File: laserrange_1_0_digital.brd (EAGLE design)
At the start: 29.5 x 54.6 mm, 32 parts, among them U1 STM32F10XRXT6

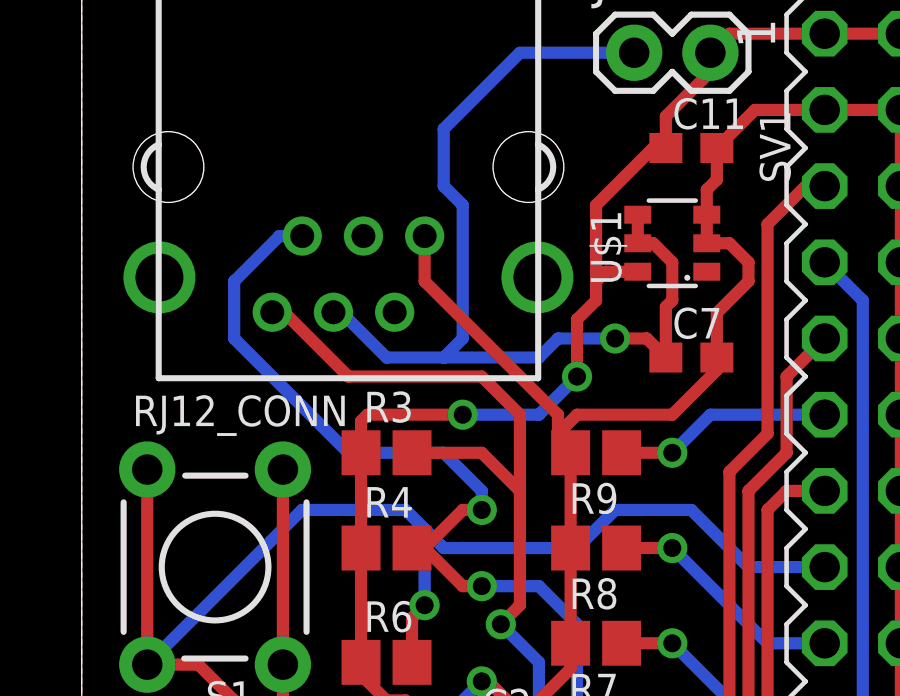
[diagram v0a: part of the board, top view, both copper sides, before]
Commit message: Fixed the RJ12 connector footpad connections
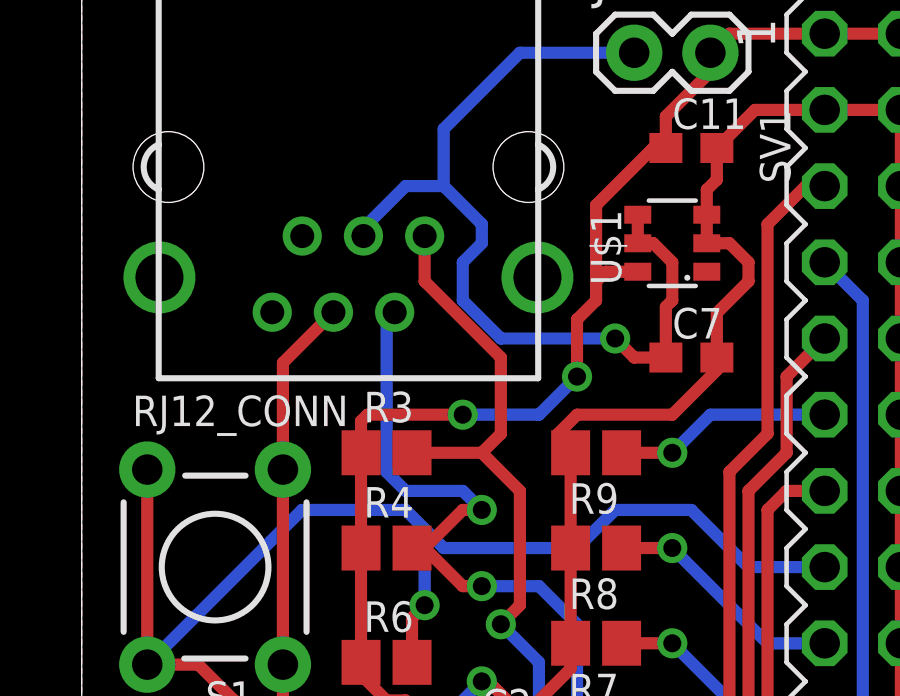
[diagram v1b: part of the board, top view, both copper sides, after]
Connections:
- net 4.3V: now also RJ12_CONN.3; no longer RJ12_CONN.4
- net GND: now also RJ12_CONN.4; no longer RJ12_CONN.1
- net I2C_CLOCK: now also RJ12_CONN.2; no longer RJ12_CONN.5
- net I2C_DATA: now also RJ12_CONN.1; no longer RJ12_CONN.6
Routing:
- net I2C_CLOCK: track 31.5 -> 24.8 mm
- net I2C_DATA: track 32.2 -> 28.6 mm
- net 4.3V: track 33.4 -> 30.6 mm
- net GND: track 173.0 -> 170.5 mm
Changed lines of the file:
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@@
 <signals>
 <signal name="4.3V">
-<contactref element="RJ12_CONN" pad="4"/>
 <contactref element="U$1" pad="5"/>
 <contactref element="C7" pad="1"/>
@@
 <wire x1="19.685" y1="43.815" x2="19.47" y2="43.6" width="0.4064" layer="1"/>
 <wire x1="19.47" y1="41.91" x2="19.47" y2="43.6" width="0.4064" layer="1"/>
-<wire x1="8.39" y1="43.42" x2="8.65" y2="43.42" width="0.4064" layer="16"/>
-<wire x1="8.65" y1="43.42" x2="10.16" y2="41.91" width="0.4064" layer="16"/>
-<wire x1="10.16" y1="41.91" x2="12.065" y2="41.91" width="0" layer="19" extent="1-16"/>
-<wire x1="10.16" y1="41.91" x2="12.065" y2="41.91" width="0.4064" layer="16"/>
-<wire x1="12.065" y1="41.91" x2="15.24" y2="41.91" width="0.4064" layer="16"/>
-<wire x1="15.24" y1="41.91" x2="15.875" y2="42.545" width="0.4064" layer="16"/>
-<wire x1="15.875" y1="42.545" x2="17.78" y2="42.545" width="0.4064" layer="16"/>
-<via x="17.78" y="42.545" extent="1-16" drill="0.6"/>
-<wire x1="17.78" y1="42.545" x2="18.835" y2="42.545" width="0.4064" layer="1"/>
-<wire x1="18.835" y1="42.545" x2="19.47" y2="41.91" width="0.4064" layer="1"/>
 <contactref element="U$1" pad="4"/>
 <wire x1="18.535" y1="45.72" x2="18.535" y2="46.67" width="0.4064" layer="1"/>
 <contactref element="JP2" pad="1"/>
+<contactref element="RJ12_CONN" pad="3"/>
+<wire x1="9.39" y1="45.96" x2="9.39" y2="46.22" width="0.4064" layer="16"/>
+<wire x1="9.39" y1="46.22" x2="10.795" y2="47.625" width="0.4064" layer="16"/>
+<wire x1="10.795" y1="47.625" x2="12.065" y2="47.625" width="0.4064" layer="16"/>
+<wire x1="12.065" y1="47.625" x2="13.335" y2="46.355" width="0.4064" layer="16"/>
+<wire x1="13.335" y1="46.355" x2="13.335" y2="45.72" width="0.4064" layer="16"/>
+<wire x1="13.335" y1="45.72" x2="12.7" y2="45.085" width="0.4064" layer="16"/>
+<wire x1="12.7" y1="45.085" x2="12.7" y2="43.815" width="0.4064" layer="16"/>
+<wire x1="12.7" y1="43.815" x2="13.97" y2="42.545" width="0.4064" layer="16"/>
+<wire x1="13.97" y1="42.545" x2="17.78" y2="42.545" width="0.4064" layer="16"/>
 <wire x1="18.415" y1="52.07" x2="14.605" y2="52.07" width="0.4064" layer="16"/>
 <wire x1="14.605" y1="52.07" x2="12.065" y2="49.53" width="0.4064" layer="16"/>
-<wire x1="12.7" y1="42.545" x2="12.065" y2="41.91" width="0" layer="19" extent="1-16"/>
 <wire x1="12.065" y1="49.53" x2="12.065" y2="47.625" width="0.4064" layer="16"/>
-<wire x1="12.065" y1="47.625" x2="12.7" y2="46.99" width="0.4064" layer="16"/>
-<wire x1="12.7" y1="46.99" x2="12.7" y2="42.545" width="0.4064" layer="16"/>
-<wire x1="12.7" y1="42.545" x2="12.065" y2="41.91" width="0.4064" layer="16"/>
-<wire x1="12.065" y1="41.91" x2="12.7" y2="42.545" width="0" layer="19" extent="1-16"/>
+<via x="17.78" y="42.545" extent="1-16" drill="0.6"/>
+<wire x1="19.47" y1="41.91" x2="18.415" y2="41.91" width="0.4064" layer="1"/>
+<wire x1="18.415" y1="41.91" x2="17.78" y2="42.545" width="0.4064" layer="1"/>
 </signal>
 <signal name="I2C_CLOCK">
-<contactref element="RJ12_CONN" pad="5"/>
 <contactref element="U1" pad="58"/>
 <contactref element="R4" pad="2"/>
@@
 <wire x1="16.51" y1="29.21" x2="16.51" y2="33.02" width="0.4064" layer="16"/>
 <via x="13.335" y="34.29" extent="1-16" drill="0.6"/>
-<wire x1="7.35" y1="45.96" x2="6.59" y2="45.96" width="0.4064" layer="16"/>
-<wire x1="6.59" y1="45.96" x2="5.08" y2="44.45" width="0.4064" layer="16"/>
-<wire x1="5.08" y1="44.45" x2="5.08" y2="42.545" width="0.4064" layer="16"/>
-<wire x1="5.08" y1="42.545" x2="8.89" y2="38.735" width="0.4064" layer="16"/>
-<wire x1="8.89" y1="38.735" x2="12.065" y2="38.735" width="0.4064" layer="16"/>
-<wire x1="12.065" y1="38.735" x2="13.335" y2="37.465" width="0.4064" layer="16"/>
 <wire x1="13.335" y1="34.29" x2="15.24" y2="34.29" width="0.4064" layer="16"/>
 <wire x1="15.24" y1="34.29" x2="16.51" y2="33.02" width="0.4064" layer="16"/>
@@
 <wire x1="11.43" y1="35.56" x2="12.7" y2="34.29" width="0.4064" layer="1"/>
 <wire x1="12.7" y1="34.29" x2="13.335" y2="34.29" width="0.4064" layer="1"/>
-<wire x1="13.335" y1="37.465" x2="13.335" y2="36.83" width="0.4064" layer="16"/>
 <via x="13.335" y="36.83" extent="1-16" drill="0.6"/>
 <wire x1="11.43" y1="35.56" x2="12.7" y2="36.83" width="0.4064" layer="1"/>
 <wire x1="12.7" y1="36.83" x2="13.335" y2="36.83" width="0.4064" layer="1"/>
+<contactref element="RJ12_CONN" pad="2"/>
+<wire x1="10.43" y1="43.42" x2="10.16" y2="43.15" width="0.4064" layer="16"/>
+<wire x1="10.16" y1="43.15" x2="10.16" y2="38.1" width="0.4064" layer="16"/>
+<wire x1="10.16" y1="38.1" x2="10.795" y2="37.465" width="0.4064" layer="16"/>
+<wire x1="10.795" y1="37.465" x2="12.7" y2="37.465" width="0.4064" layer="16"/>
+<wire x1="12.7" y1="37.465" x2="13.335" y2="36.83" width="0.4064" layer="16"/>
 </signal>
 <signal name="I2C_DATA">
-<contactref element="RJ12_CONN" pad="6"/>
 <contactref element="U1" pad="59"/>
 <contactref element="R3" pad="2"/>
@@
 <via x="13.97" y="33.02" extent="1-16" drill="0.6"/>
 <wire x1="15.875" y1="27.94" x2="15.875" y2="24.765" width="0.4064" layer="16"/>
-<wire x1="6.35" y1="43.42" x2="6.745" y2="43.42" width="0.4064" layer="1"/>
-<wire x1="14.605" y1="37.465" x2="14.605" y2="40.005" width="0.4064" layer="1"/>
-<wire x1="14.605" y1="40.005" x2="13.335" y2="41.275" width="0.4064" layer="1"/>
-<wire x1="13.335" y1="41.275" x2="8.89" y2="41.275" width="0.4064" layer="1"/>
-<wire x1="8.89" y1="41.275" x2="6.745" y2="43.42" width="0.4064" layer="1"/>
 <wire x1="15.875" y1="27.94" x2="15.24" y2="28.575" width="0.4064" layer="16"/>
 <wire x1="15.24" y1="28.575" x2="15.24" y2="31.75" width="0.4064" layer="16"/>
 <wire x1="15.24" y1="31.75" x2="13.97" y2="33.02" width="0.4064" layer="16"/>
+<contactref element="RJ12_CONN" pad="1"/>
+<wire x1="11.43" y1="45.96" x2="11.43" y2="44.45" width="0.4064" layer="1"/>
+<wire x1="11.43" y1="44.45" x2="13.97" y2="41.91" width="0.4064" layer="1"/>
+<wire x1="13.97" y1="41.91" x2="13.97" y2="39.37" width="0.4064" layer="1"/>
+<wire x1="13.97" y1="39.37" x2="13.335" y2="38.735" width="0.4064" layer="1"/>
 </signal>
 <signal name="GND">
-<contactref element="RJ12_CONN" pad="1"/>
 <contactref element="U1" pad="31"/>
 <contactref element="U1" pad="47"/>
@@
 <wire x1="6.35" y1="24.13" x2="6.35" y2="19.685" width="0.4064" layer="16"/>
 <wire x1="6.35" y1="19.685" x2="8.255" y2="17.78" width="0.4064" layer="16"/>
-<wire x1="11.43" y1="45.96" x2="11.43" y2="44.45" width="0.4064" layer="1"/>
-<wire x1="11.43" y1="44.45" x2="15.875" y2="40.005" width="0.4064" layer="1"/>
-<wire x1="15.875" y1="40.005" x2="15.875" y2="39.37" width="0.4064" layer="1"/>
 <wire x1="15.875" y1="39.37" x2="15.875" y2="39.155" width="0.4064" layer="1"/>
 <wire x1="15.875" y1="39.155" x2="16.295" y2="38.735" width="0.4064" layer="1"/>
@@
 <wire x1="24.765" y1="50.165" x2="22.44" y2="50.165" width="0.4064" layer="1"/>
 <wire x1="22.44" y1="50.165" x2="21.17" y2="48.895" width="0.4064" layer="1"/>
+<contactref element="RJ12_CONN" pad="4"/>
+<wire x1="6.7056" y1="38.1762" x2="6.7056" y2="41.7356" width="0.4064" layer="1"/>
+<wire x1="6.7056" y1="41.7356" x2="8.39" y2="43.42" width="0.4064" layer="1"/>
 </signal>
 <signal name="N$1">
